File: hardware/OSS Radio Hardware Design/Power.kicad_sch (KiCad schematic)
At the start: 51 parts, among them J7 BATT_CONN, Q2 AO3401A, Q3 AO3400A, Q4 AO3400A, Q5 AO3400A, Q6 AO3400A, U10 LM5157RTER, U13 NCP1117-1.8_SOT223, U2 S-8252ACP-M6T1U, U3 NCP1117-3.3_SOT223, U9 MCP73844-840I/MS

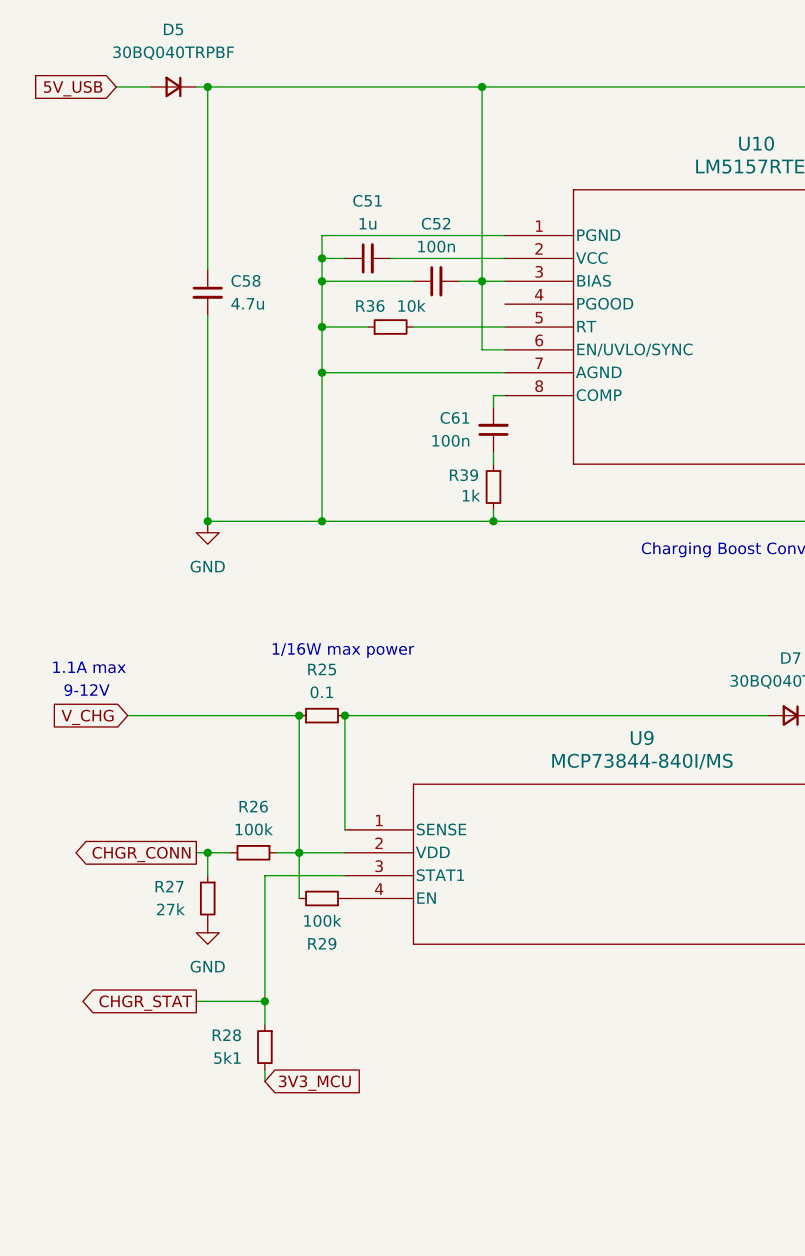
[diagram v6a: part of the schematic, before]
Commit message: added ESD diodes, MARS resistor, Charge LED, Status LED
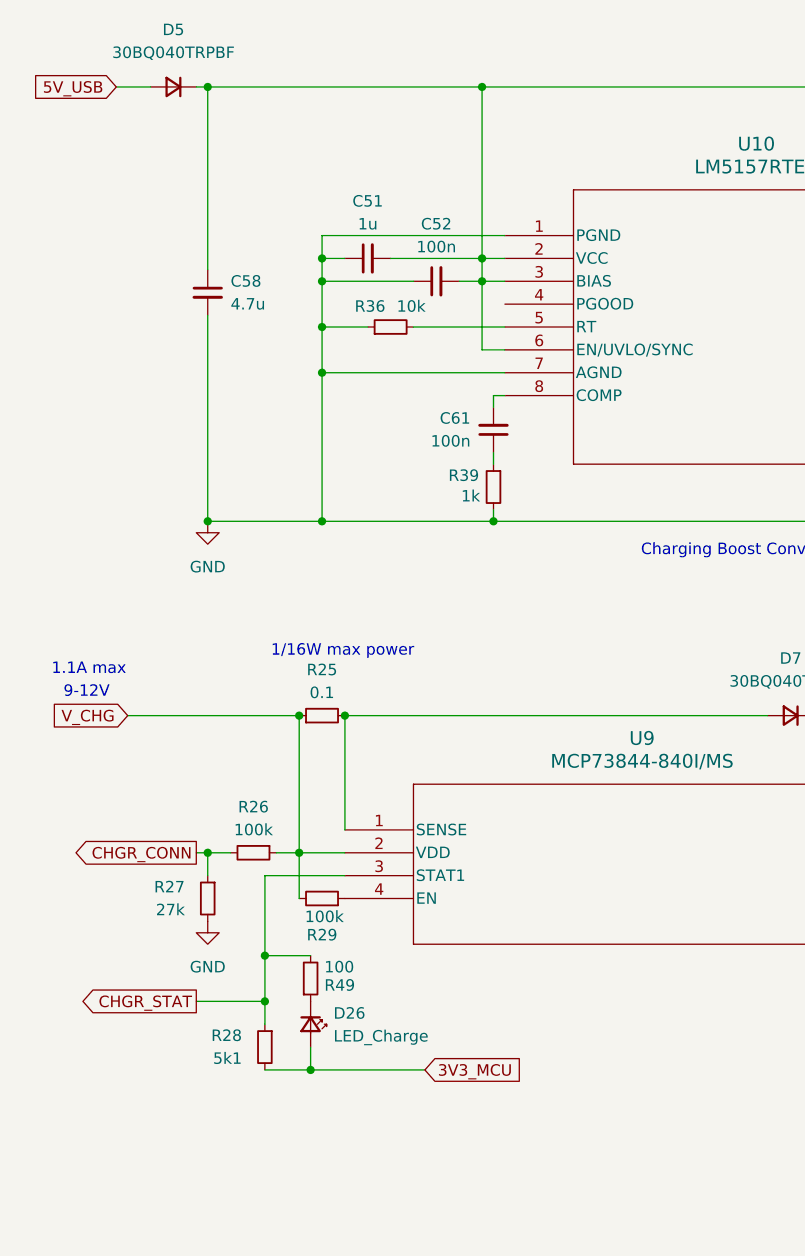
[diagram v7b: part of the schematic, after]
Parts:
- added D26: LED_Charge, symbol Device:LED_Small
- added R49: 100, symbol Device:R_Small
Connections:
- net 3V3_MCU: now also D26.2 (A)
- net CHGR_STAT: now also R49.2
- net at C51.2, U10.2 (VCC): now also C52.2, C58.1, D5.1 (K), L3.1, U10.3 (BIAS), U10.6 (EN/UVLO/SYNC)
- new net: D26.1 (K), R49.1
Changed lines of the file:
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@@
 	)
 	(junction
+		(at 48.26 130.81)
+		(diameter 0)
+		(color 0 0 0 0)
+	)
+	(junction
 		(at 212.09 25.4)
 		(diameter 0)
@@
 	)
 	(junction
+		(at 67.31 40.64)
+		(diameter 0)
+		(color 0 0 0 0)
+	)
+	(junction
 		(at 246.38 132.08)
 		(diameter 0)
@@
 	)
 	(junction
+		(at 43.18 118.11)
+		(diameter 0)
+		(color 0 0 0 0)
+	)
+	(junction
 		(at 135.89 45.72)
 		(diameter 0)
@@
 	(wire
 		(pts
+			(xy 67.31 40.64) (xy 67.31 43.18)
+		)
+		(stroke
+			(width 0)
+			(type default)
+		)
+	)
+	(wire
+		(pts
 			(xy 152.4 151.13) (xy 166.37 151.13)
 		)
@@
 	(wire
 		(pts
+			(xy 60.96 130.81) (xy 48.26 130.81)
+		)
+		(stroke
+			(width 0)
+			(type default)
+		)
+	)
+	(wire
+		(pts
 			(xy 157.48 59.69) (xy 157.48 69.85)
 		)
@@
 	(wire
 		(pts
+			(xy 48.26 130.81) (xy 43.18 130.81)
+		)
+		(stroke
+			(width 0)
+			(type default)
+		)
+	)
+	(wire
+		(pts
 			(xy 147.32 45.72) (xy 149.86 45.72)
 		)
@@
 	(wire
 		(pts
+			(xy 57.15 40.64) (xy 67.31 40.64)
+		)
+		(stroke
+			(width 0)
+			(type default)
+		)
+	)
+	(wire
+		(pts
 			(xy 246.38 132.08) (xy 246.38 133.35)
 		)
@@
 	(wire
 		(pts
+			(xy 67.31 21.59) (xy 67.31 40.64)
+		)
+		(stroke
+			(width 0)
+			(type default)
+		)
+	)
+	(wire
+		(pts
+			(xy 43.18 118.11) (xy 48.26 118.11)
+		)
+		(stroke
+			(width 0)
+			(type default)
+		)
+	)
+	(wire
+		(pts
 			(xy 49.53 48.26) (xy 54.61 48.26)
 		)
@@
 	(wire
 		(pts
-			(xy 67.31 21.59) (xy 67.31 43.18)
-		)
-		(stroke
-			(width 0)
-			(type default)
-		)
-	)
-	(wire
-		(pts
 			(xy 67.31 21.59) (xy 109.22 21.59)
 		)
@@
 	(wire
 		(pts
-			(xy 57.15 40.64) (xy 69.85 40.64)
-		)
-		(stroke
-			(width 0)
-			(type default)
-		)
-	)
-	(wire
-		(pts
 			(xy 142.24 99.06) (xy 133.35 99.06)
 		)
@@
 	(wire
 		(pts
-			(xy 43.18 109.22) (xy 43.18 123.19)
+			(xy 43.18 109.22) (xy 43.18 118.11)
 		)
 		(stroke
@@
 	(wire
 		(pts
+			(xy 48.26 128.27) (xy 48.26 130.81)
+		)
+		(stroke
+			(width 0)
+			(type default)
+		)
+	)
+	(wire
+		(pts
 			(xy 128.27 111.76) (xy 133.35 111.76)
 		)
@@
 	(wire
 		(pts
+			(xy 67.31 40.64) (xy 69.85 40.64)
+		)
+		(stroke
+			(width 0)
+			(type default)
+		)
+	)
+	(wire
+		(pts
 			(xy 49.53 40.64) (xy 52.07 40.64)
 		)
@@
 	(wire
 		(pts
+			(xy 43.18 118.11) (xy 43.18 123.19)
+		)
+		(stroke
+			(width 0)
+			(type default)
+		)
+	)
+	(wire
+		(pts
 			(xy 152.4 116.84) (xy 152.4 125.73)
 		)
@@
 	(wire
 		(pts
-			(xy 43.18 130.81) (xy 43.18 132.08)
-		)
-		(stroke
-			(width 0)
-			(type default)
-		)
-	)
-	(wire
-		(pts
 			(xy 157.48 69.85) (xy 149.86 69.85)
 		)
@@
 	(global_label "3V3_MCU"
 		(shape input)
-		(at 43.18 132.08 0)
+		(at 60.96 130.81 0)
 		(fields_autoplaced yes)
 		(effects
@@
 		)
 		(property "Intersheetrefs" "${INTERSHEET_REFS}"
-			(at 54.6923 132.08 0)
+			(at 72.4723 130.81 0)
 			(effects
 				(font
@@
 	)
 	(symbol
+		(lib_id "Device:R_Small")
+		(at 48.26 120.65 0)
+		(mirror x)
+		(unit 1)
+		(exclude_from_sim no)
+		(in_bom yes)
+		(on_board yes)
+		(dnp no)
+		(property "Reference" "R49"
+			(at 49.784 121.412 0)
+			(effects
+				(font
+					(size 1.27 1.27)
+				)
+				(justify left)
+			)
+		)
+		(property "Value" "100"
+			(at 49.784 119.38 0)
+			(effects
+				(font
+					(size 1.27 1.27)
+				)
+				(justify left)
+			)
+		)
+		(property "Footprint" ""
+			(at 48.26 120.65 0)
+			(effects
+				(font
+					(size 1.27 1.27)
+				)
+				(hide yes)
+			)
+		)
+		(property "Datasheet" "~"
+			(at 48.26 120.65 0)
+			(effects
+				(font
+					(size 1.27 1.27)
+				)
+				(hide yes)
+			)
+		)
+		(property "Description" "Resistor, small symbol"
+			(at 48.26 120.65 0)
+			(effects
+				(font
+					(size 1.27 1.27)
+				)
+				(hide yes)
+			)
+		)
+		(pin "1"
+		)
+		(pin "2"
+		)
+		(instances
+			(project "OSS Radio Hardware Design"
+				(path "/fd5c68a7-f5d0-4135-a258-bde3ebf63307/c701d20d-e266-4c46-aeb3-ff3d813a359d"
+					(reference "R49")
+					(unit 1)
+				)
+			)
+		)
+	)
+	(symbol
 		(lib_id "Device:R")
 		(at 203.2 45.72 270)
@@
 		(dnp no)
 		(property "Reference" "R29"
-			(at 49.53 116.84 90)
+			(at 49.53 115.824 90)
 			(effects
 				(font
@@
 		)
 		(property "Value" "100k"
-			(at 49.53 114.3 90)
+			(at 49.784 113.792 90)
 			(effects
 				(font
@@
 					(unit 1)
 				)
+			)
+		)
+	)
+	(symbol
+		(lib_id "Device:LED_Small")
+		(at 48.26 125.73 270)
+		(unit 1)
+		(exclude_from_sim no)
+		(in_bom yes)
+		(on_board yes)
+		(dnp no)
+		(fields_autoplaced yes)
+		(property "Reference" "D26"
+			(at 50.8 124.5234 90)
+			(effects
+				(font
+					(size 1.27 1.27)
+				)
+				(justify left)
+			)
+		)
+		(property "Value" "LED_Charge"
+			(at 50.8 127.0634 90)
+			(effects
+				(font
+					(size 1.27 1.27)
+				)
+				(justify left)
+			)
+		)
+		(property "Footprint" ""
+			(at 48.26 125.73 90)
+			(effects
+				(font
+					(size 1.27 1.27)
+				)
+				(hide yes)
+			)
+		)
+		(property "Datasheet" "~"
+			(at 48.26 125.73 90)
+			(effects
+				(font
+					(size 1.27 1.27)
+				)
+				(hide yes)
+			)
+		)
+		(property "Description" "Light emitting diode, small symbol"
+			(at 48.26 125.73 0)
+			(effects
+				(font
+					(size 1.27 1.27)
+				)
+				(hide yes)
+			)
+		)
+		(property "Sim.Pin" "1=K 2=A"
+			(at 48.26 125.73 0)
+			(effects
+				(font
+					(size 1.27 1.27)
+				)
+				(hide yes)
+			)
+		)
+		(pin "1"
+		)
+		(pin "2"
+		)
+		(instances
+			(project "OSS Radio Hardware Design"
+				(path "/fd5c68a7-f5d0-4135-a258-bde3ebf63307/c701d20d-e266-4c46-aeb3-ff3d813a359d"
+					(reference "D26")
+					(unit 1)
+				)

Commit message: working on fooprints
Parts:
- C48, C5, C50, C51, C53, C58, C6, C60, C63, C64, C65, C69: footprint (none) -> Capacitor_SMD:C_0603_1608Metric_Pad1.08x0.95mm_HandSolder
- C52, C55, C56, C57, C59, C61: footprint (none) -> Capacitor_SMD:C_0402_1005Metric_Pad0.74x0.62mm_HandSolder
- C54: footprint (none) -> Capacitor_SMD:C_1206_3216Metric_Pad1.33x1.80mm_HandSolder
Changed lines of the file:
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@@
 			)
 		)
-		(property "Footprint" ""
+		(property "Footprint" "Capacitor_SMD:C_0603_1608Metric_Pad1.08x0.95mm_HandSolder"
 			(at 133.35 93.98 0)
 			(effects
@@
 			)
 		)
-		(property "Footprint" ""
+		(property "Footprint" "Capacitor_SMD:C_0603_1608Metric_Pad1.08x0.95mm_HandSolder"
 			(at 245.4148 52.07 0)
 			(effects
@@
 			)
 		)
-		(property "Footprint" ""
+		(property "Footprint" "Capacitor_SMD:C_0603_1608Metric_Pad1.08x0.95mm_HandSolder"
 			(at 255.5748 52.07 0)
 			(effects
@@
 			)
 		)
-		(property "Footprint" ""
+		(property "Footprint" "Capacitor_SMD:C_0402_1005Metric_Pad0.74x0.62mm_HandSolder"
 			(at 222.25 139.7 0)
 			(effects
@@
 			)
 		)
-		(property "Footprint" ""
+		(property "Footprint" "Capacitor_SMD:C_0402_1005Metric_Pad0.74x0.62mm_HandSolder"
 			(at 125.73 111.76 0)
 			(effects
@@
 			)
 		)
-		(property "Footprint" ""
+		(property "Footprint" "Capacitor_SMD:C_0603_1608Metric_Pad1.08x0.95mm_HandSolder"
 			(at 211.1248 52.07 0)
 			(effects
@@
 			)
 		)
-		(property "Footprint" ""
+		(property "Footprint" "Capacitor_SMD:C_0603_1608Metric_Pad1.08x0.95mm_HandSolder"
 			(at 156.5148 52.07 0)
 			(effects
@@
 			)
 		)
-		(property "Footprint" ""
+		(property "Footprint" "Capacitor_SMD:C_0603_1608Metric_Pad1.08x0.95mm_HandSolder"
 			(at 54.61 40.64 0)
 			(effects
@@
 			)
 		)
-		(property "Footprint" ""
+		(property "Footprint" "Capacitor_SMD:C_0402_1005Metric_Pad0.74x0.62mm_HandSolder"
 			(at 222.25 134.62 0)
 			(effects
@@
 			)
 		)
-		(property "Footprint" ""
+		(property "Footprint" "Capacitor_SMD:C_0402_1005Metric_Pad0.74x0.62mm_HandSolder"
 			(at 132.08 63.5 0)
 			(effects
@@
 			)
 		)
-		(property "Footprint" ""
+		(property "Footprint" "Capacitor_SMD:C_0603_1608Metric_Pad1.08x0.95mm_HandSolder"
 			(at 222.5548 25.4 0)
 			(effects
@@
 			)
 		)
-		(property "Footprint" ""
+		(property "Footprint" "Capacitor_SMD:C_0603_1608Metric_Pad1.08x0.95mm_HandSolder"
 			(at 255.5748 25.4 0)
 			(effects
@@
 			)
 		)
-		(property "Footprint" ""
+		(property "Footprint" "Capacitor_SMD:C_0603_1608Metric_Pad1.08x0.95mm_HandSolder"
 			(at 211.1248 25.4 0)
 			(effects
@@
 			)
 		)
-		(property "Footprint" ""
+		(property "Footprint" "Capacitor_SMD:C_0603_1608Metric_Pad1.08x0.95mm_HandSolder"
 			(at 36.83 44.45 0)
 			(effects
@@
 			)
 		)
-		(property "Footprint" ""
+		(property "Footprint" "Capacitor_SMD:C_0402_1005Metric_Pad0.74x0.62mm_HandSolder"
 			(at 62.23 43.18 0)
 			(effects
@@
 			)
 		)
-		(property "Footprint" ""
+		(property "Footprint" "Capacitor_SMD:C_1206_3216Metric_Pad1.33x1.80mm_HandSolder"
 			(at 142.24 93.98 0)
 			(effects
@@
 			)
 		)
-		(property "Footprint" ""
+		(property "Footprint" "Capacitor_SMD:C_0402_1005Metric_Pad0.74x0.62mm_HandSolder"
 			(at 68.58 59.69 0)
 			(effects
@@
 			)
 		)
-		(property "Footprint" ""
+		(property "Footprint" "Capacitor_SMD:C_0603_1608Metric_Pad1.08x0.95mm_HandSolder"
 			(at 222.5548 52.07 0)
 			(effects
@@
 			)
 		)
-		(property "Footprint" ""
+		(property "Footprint" "Capacitor_SMD:C_0603_1608Metric_Pad1.08x0.95mm_HandSolder"
 			(at 245.4148 25.4 0)
 			(effects
